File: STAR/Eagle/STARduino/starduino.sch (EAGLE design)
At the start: 80 parts, among them J3 J30J-15J30, J4 J30J-31J30, Q2 BSS8402DW, Q3 BSS8402DW, U1 SSCMNNN015PA2A3, U10 MC14504BDTG, U11 MAX31725MTA+, U12 TCA9535_RTW_24, U13 BMX055, U15 MC74VHC1GT125, U16 PCA9515A, U17 PCA9306DCT, U18 LT8616, U4 DS3231MZ+, U6 ATSAMD21G18, U8 ADXL375BCCZ

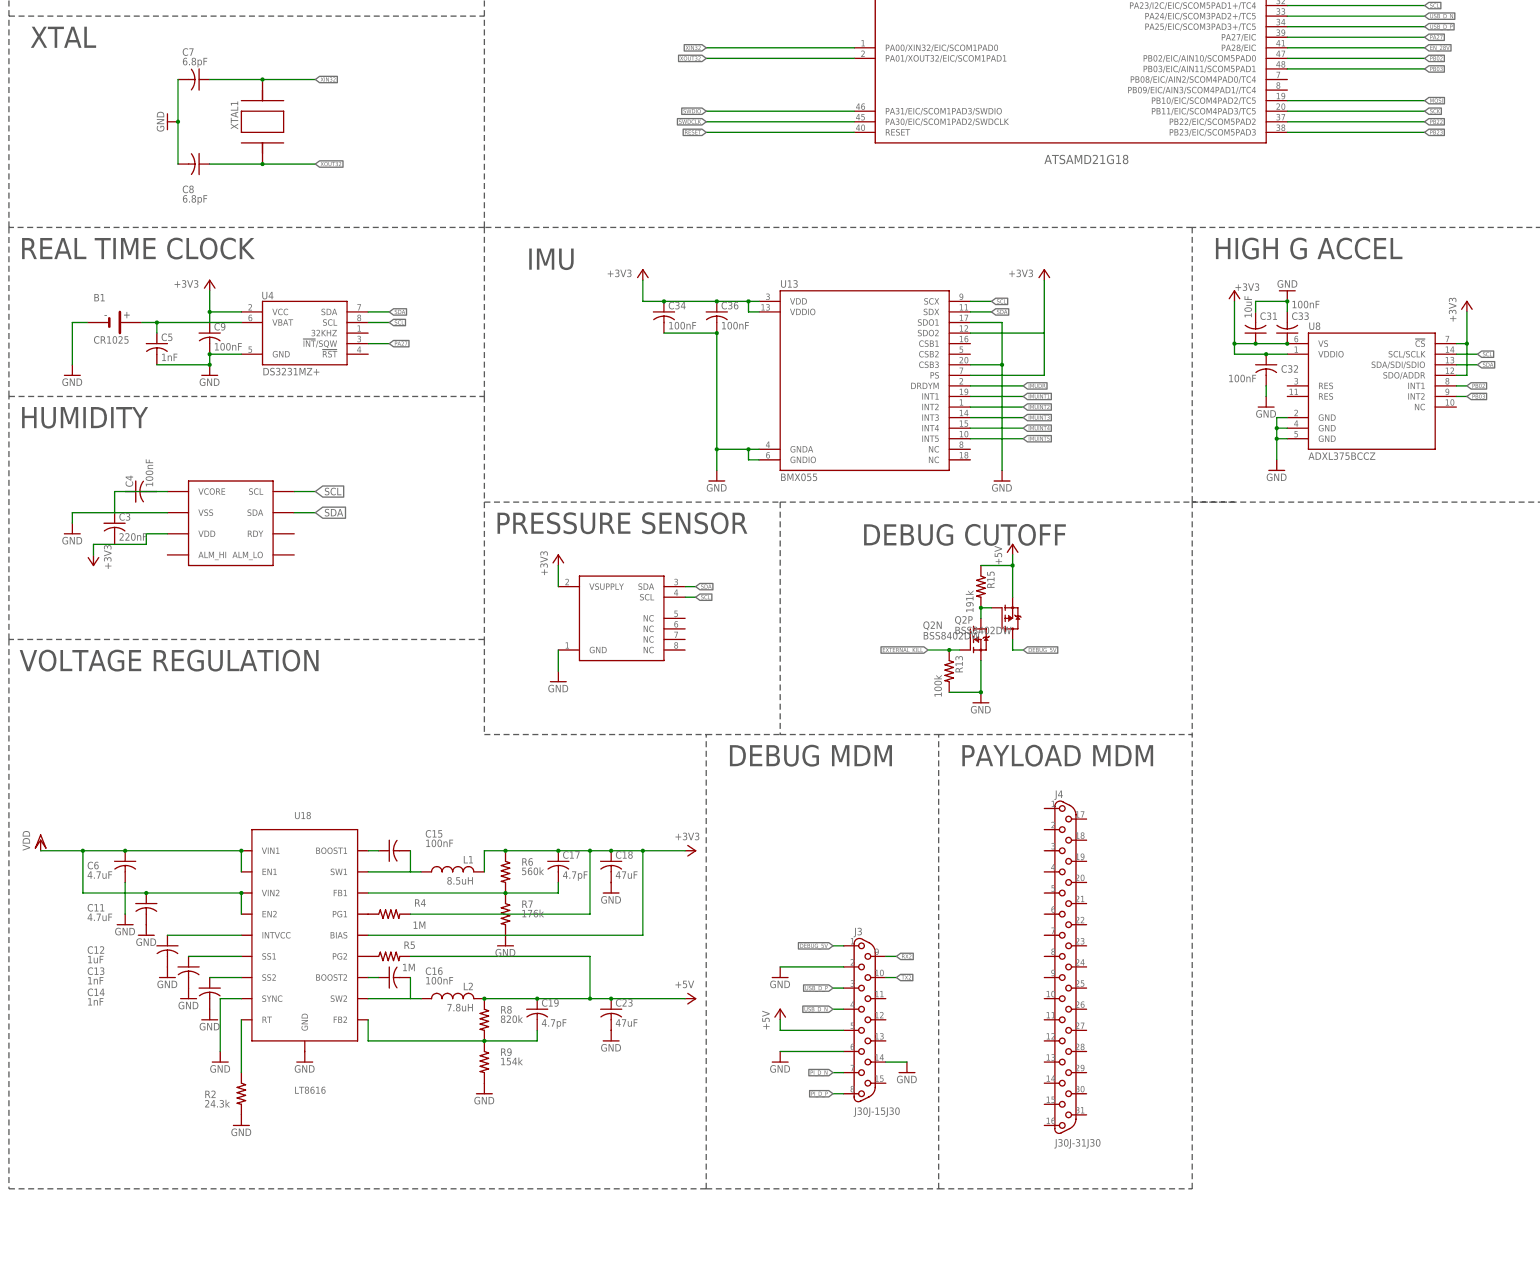
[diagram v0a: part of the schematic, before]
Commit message: datalogger differential pairs
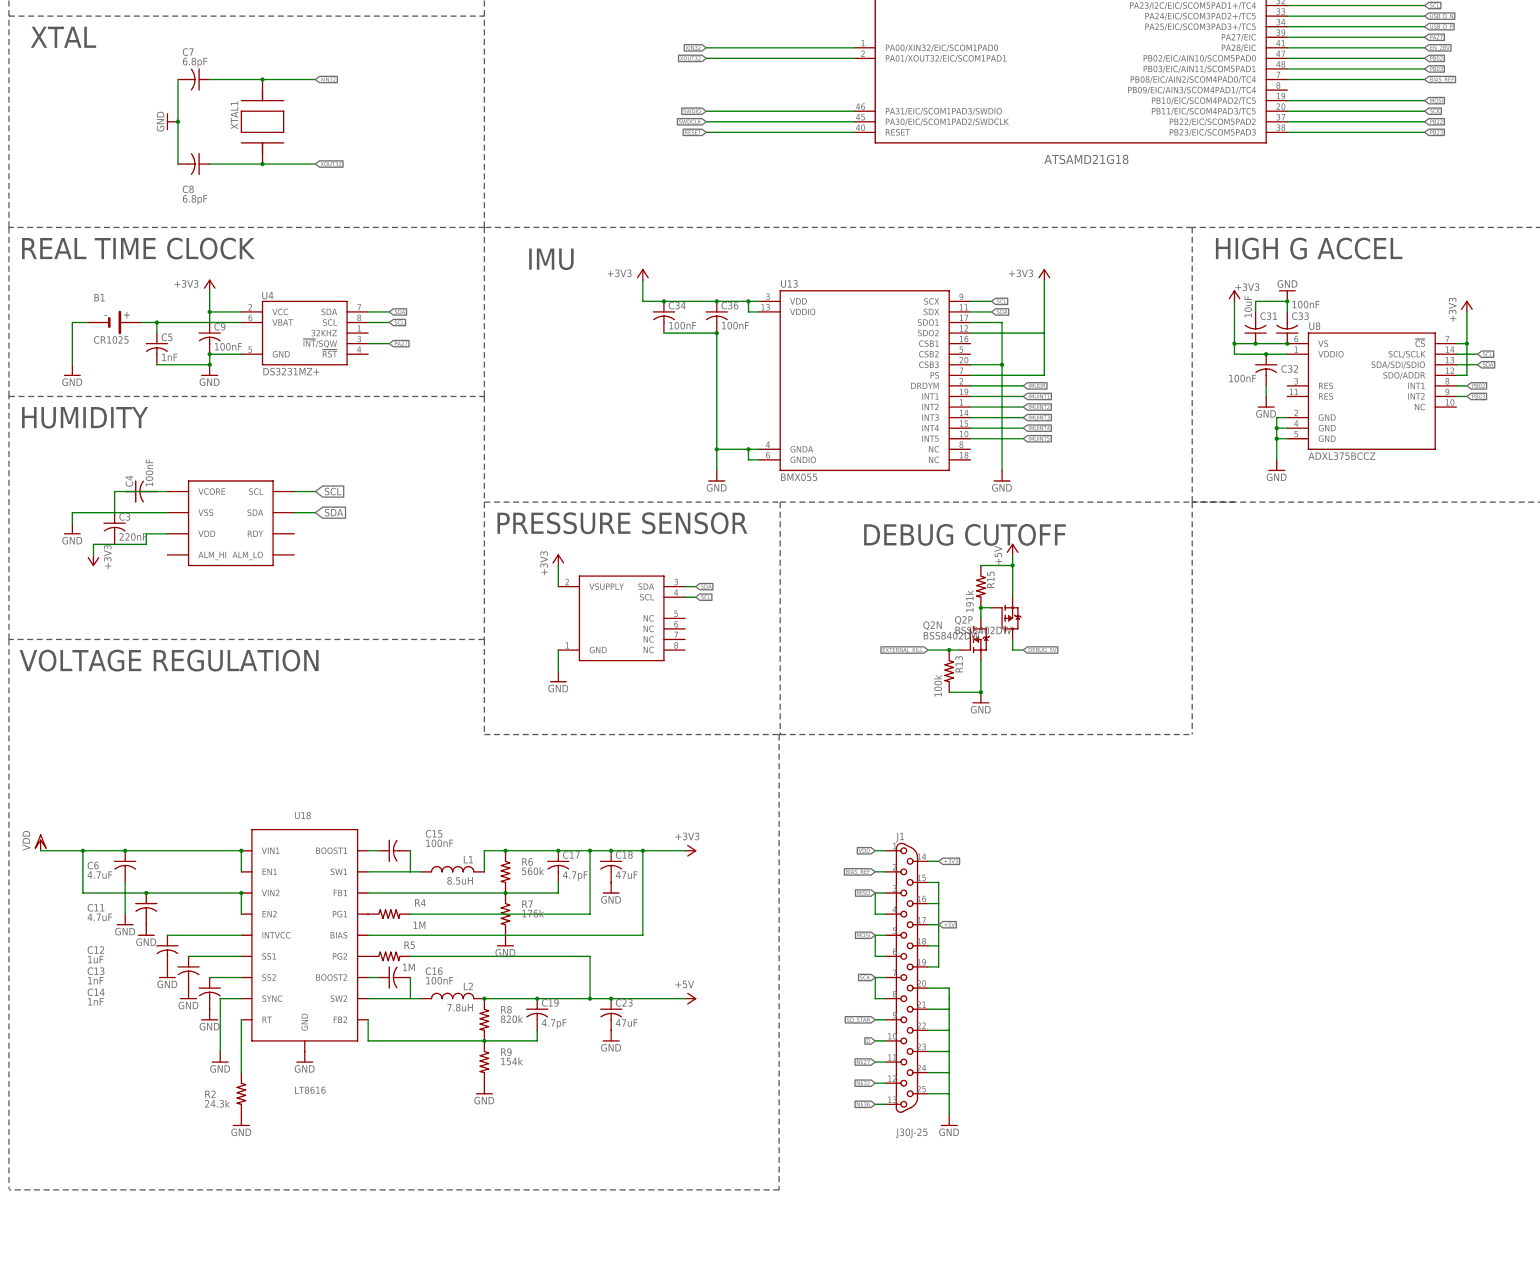
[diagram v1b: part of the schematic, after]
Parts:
- removed J3: J30J-15J30, CM_J30J:J30J-15J30
- removed J4: J30J-31J30, CM_J30J:J30J-31J30
- added J1: J30J-25, CM_J30J:J30J-25
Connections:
- removed net PI_D_N: J3.7
- removed net PI_D_P: J3.8
- new net BIAS_REF: J1.2, U6.PB08/EIC/AIN2/SCOM4PAD0/TC4
- new net D: J1.10
- new net N$27: J1.11
- new net N$32: J1.12
- new net N$36: J1.13
- new net SD_STAR: J1.9
- net +3V3: now also J1.14
- net +5V: now also J1.15, J1.16, J1.17, J1.18, J1.19; no longer J3.5
- net DEBUG_5V: no longer J3.1
- net GND: now also J1.20, J1.21, J1.22, J1.23, J1.24, J1.25; no longer J3.14, J3.2, J3.6
- net MISO: now also J1.3, J1.4
- net MOSI: now also J1.5, J1.6
- net RX2: no longer J3.9
- net SCK: now also J1.7, J1.8
- net TX2: no longer J3.10
- net USB_D_N: no longer J3.4
- net USB_D_P: no longer J3.3
- net VDD: now also J1.1
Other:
- note removed: "DEBUG MDM"
- note removed: "PAYLOAD MDM"

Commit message: got rid of old STARduino routing
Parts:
- removed Q3: BSS8402DW, transistor-fet:BSS8402DW
- removed R22: 100k, resistor:R-US_R0603
- removed R24: 191k, resistor:R-US_R0603
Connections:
- removed net EXTERNAL_3V3: Q3P.D
- removed net N$18: Q3N.D, Q3P.G, R24.2
- new net N$2: C4.2, U$3.VCORE
- net +3V3: no longer Q3P.S, R24.1
- net EXTERNAL_KILL: no longer Q3N.G, R22.1
- net GND: no longer C4.2, Q3N.S, R22.2, U$3.VCORE
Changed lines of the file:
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@@
 <part name="GND10" library="supply1" deviceset="GND" device=""/>
 <part name="+3V9" library="supply1" deviceset="+3V3" device=""/>
-<part name="+3V19" library="supply1" deviceset="+3V3" device=""/>
-<part name="GND22" library="supply1" deviceset="GND" device=""/>
-<part name="R22" library="resistor" deviceset="R-US_" device="R0603" value="100k"/>
-<part name="R24" library="resistor" deviceset="R-US_" device="R0603" value="191k"/>
 <part name="JP1" library="CM_passives" deviceset="JUMPER-2" device="PTH"/>
 <part name="U$2" library="images" deviceset="SSL" device=".3IN_SILK"/>
 <part name="U$1" library="images" deviceset="STAR" device=""/>
 <part name="R28" library="SparkFun-Passives" deviceset="RESISTOR-ARRAY" device="0603-ARV" value="4.7k"/>
-<part name="Q3" library="transistor-fet" deviceset="BSS8402DW" device=""/>
 <part name="Q2" library="transistor-fet" deviceset="BSS8402DW" device=""/>
 <part name="U16" library="CM_IC" deviceset="PCA9515A" device=""/>
@@
 <instance part="GND10" gate="1" x="533.4" y="375.92"/>
 <instance part="+3V9" gate="G$1" x="505.46" y="355.6"/>
-<instance part="+3V19" gate="G$1" x="436.88" y="314.96" rot="R90"/>
-<instance part="GND22" gate="1" x="459.74" y="297.18"/>
-<instance part="R22" gate="G$1" x="449.58" y="299.72" rot="R270"/>
-<instance part="R24" gate="G$1" x="469.9" y="307.34" rot="R270"/>
 <instance part="JP1" gate="A" x="43.18" y="365.76"/>
 <instance part="U$2" gate="G$1" x="546.1" y="48.26"/>
@@
 <instance part="R28" gate="C" x="391.16" y="304.8" rot="R90"/>
 <instance part="R28" gate="D" x="416.56" y="304.8" rot="R90"/>
-<instance part="Q3" gate="N" x="457.2" y="307.34"/>
-<instance part="Q3" gate="P" x="482.6" y="307.34"/>
 <instance part="Q2" gate="N" x="236.22" y="193.04"/>
 <instance part="Q2" gate="P" x="243.84" y="198.12"/>
@@
 <pinref part="R28" gate="A" pin="2"/>
 <pinref part="R28" gate="B" pin="2"/>
-</segment>
-<segment>
-<pinref part="+3V19" gate="G$1" pin="+3V3"/>
-<wire x1="439.42" y1="314.96" x2="469.9" y2="314.96" width="0.1524" layer="91"/>
-<wire x1="469.9" y1="314.96" x2="485.14" y2="314.96" width="0.1524" layer="91"/>
-<wire x1="485.14" y1="314.96" x2="485.14" y2="312.42" width="0.1524" layer="91"/>
-<pinref part="R24" gate="G$1" pin="1"/>
-<wire x1="469.9" y1="314.96" x2="469.9" y2="312.42" width="0.1524" layer="91"/>
-<junction x="469.9" y="314.96"/>
-<pinref part="Q3" gate="P" pin="S"/>
 </segment>
 <segment>
@@
 </segment>
 <segment>
-<pinref part="GND22" gate="1" pin="GND"/>
-<wire x1="459.74" y1="302.26" x2="459.74" y2="299.72" width="0.1524" layer="91"/>
-<pinref part="R22" gate="G$1" pin="2"/>
-<wire x1="449.58" y1="294.64" x2="454.66" y2="294.64" width="0.1524" layer="91"/>
-<wire x1="454.66" y1="294.64" x2="454.66" y2="302.26" width="0.1524" layer="91"/>
-<wire x1="454.66" y1="302.26" x2="459.74" y2="302.26" width="0.1524" layer="91"/>
-<pinref part="Q3" gate="N" pin="S"/>
-<junction x="459.74" y="302.26"/>
-</segment>
-<segment>
 <pinref part="C41" gate="G$1" pin="2"/>
 <pinref part="GND15" gate="1" pin="GND"/>
@@
 <wire x1="20.32" y1="223.52" x2="20.32" y2="220.98" width="0.1524" layer="91"/>
 <pinref part="GND13" gate="1" pin="GND"/>
-<pinref part="U$3" gate="G$1" pin="VCORE"/>
-<pinref part="C4" gate="G$1" pin="2"/>
-<wire x1="43.18" y1="228.6" x2="40.64" y2="228.6" width="0.1524" layer="91"/>
 <pinref part="C4" gate="G$1" pin="1"/>
-<wire x1="40.64" y1="228.6" x2="33.02" y2="228.6" width="0.1524" layer="91"/>
 <wire x1="33.02" y1="228.6" x2="30.48" y2="228.6" width="0.1524" layer="91"/>
 <wire x1="30.48" y1="228.6" x2="30.48" y2="223.52" width="0.1524" layer="91"/>
@@
 </segment>
 <segment>
-<pinref part="R22" gate="G$1" pin="1"/>
-<wire x1="454.66" y1="304.8" x2="449.58" y2="304.8" width="0.1524" layer="91"/>
-<wire x1="449.58" y1="304.8" x2="447.04" y2="304.8" width="0.1524" layer="91"/>
-<junction x="449.58" y="304.8"/>
-<label x="447.04" y="304.8" size="1.016" layer="95" rot="R180" xref="yes"/>
-<pinref part="Q3" gate="N" pin="G"/>
-</segment>
-<segment>
 <pinref part="U16" gate="G$1" pin="EN"/>
 <wire x1="500.38" y1="381" x2="497.84" y2="381" width="0.1524" layer="91"/>
@@
 <label x="508" y="340.36" size="1.016" layer="95" xref="yes"/>
 <pinref part="R28" gate="A" pin="1"/>
-</segment>
-</net>
-<net name="N$18" class="0">
-<segment>
-<wire x1="459.74" y1="312.42" x2="464.82" y2="312.42" width="0.1524" layer="91"/>
-<wire x1="464.82" y1="312.42" x2="464.82" y2="299.72" width="0.1524" layer="91"/>
-<pinref part="R24" gate="G$1" pin="2"/>
-<wire x1="464.82" y1="299.72" x2="469.9" y2="299.72" width="0.1524" layer="91"/>
-<wire x1="469.9" y1="299.72" x2="469.9" y2="302.26" width="0.1524" layer="91"/>
-<wire x1="469.9" y1="299.72" x2="480.06" y2="299.72" width="0.1524" layer="91"/>
-<wire x1="480.06" y1="299.72" x2="480.06" y2="309.88" width="0.1524" layer="91"/>
-<junction x="469.9" y="299.72"/>
-<pinref part="Q3" gate="P" pin="G"/>
-<pinref part="Q3" gate="N" pin="D"/>
-</segment>
-</net>
-<net name="EXTERNAL_3V3" class="0">
-<segment>
-<wire x1="485.14" y1="302.26" x2="485.14" y2="299.72" width="0.1524" layer="91"/>
-<wire x1="485.14" y1="299.72" x2="490.22" y2="299.72" width="0.1524" layer="91"/>
-<label x="490.22" y="299.72" size="1.016" layer="95" xref="yes"/>
-<pinref part="Q3" gate="P" pin="D"/>
 </segment>
 </net>
@@
 </segment>
 </net>
+<net name="N$2" class="0">
+<segment>
+<pinref part="C4" gate="G$1" pin="2"/>
+<pinref part="U$3" gate="G$1" pin="VCORE"/>
+<wire x1="43.18" y1="228.6" x2="40.64" y2="228.6" width="0.1524" layer="91"/>
+</segment>
+</net>

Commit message: half a routed STARduino
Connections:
- removed net N$13: C15.2
- removed net N$16: C16.2
- net GND: now also C3.1
- net N$14: now also C15.2
- net N$17: now also C16.2
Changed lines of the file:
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@@
 <wire x1="33.02" y1="228.6" x2="30.48" y2="228.6" width="0.1524" layer="91"/>
 <wire x1="30.48" y1="228.6" x2="30.48" y2="223.52" width="0.1524" layer="91"/>
+<pinref part="C3" gate="G$1" pin="1"/>
 </segment>
 <segment>
@@
 </segment>
 </net>
-<net name="N$13" class="0">
-<segment>
+<net name="N$14" class="0">
+<segment>
+<pinref part="U18" gate="G$1" pin="SW1"/>
+<wire x1="91.44" y1="137.16" x2="101.6" y2="137.16" width="0.1524" layer="91"/>
+<pinref part="L1" gate="G$1" pin="1"/>
 <pinref part="C15" gate="G$1" pin="2"/>
+<wire x1="101.6" y1="137.16" x2="104.14" y2="137.16" width="0.1524" layer="91"/>
 <wire x1="101.6" y1="142.24" x2="101.6" y2="137.16" width="0.1524" layer="91"/>
 </segment>
 </net>
-<net name="N$14" class="0">
-<segment>
-<pinref part="U18" gate="G$1" pin="SW1"/>
-<wire x1="91.44" y1="137.16" x2="104.14" y2="137.16" width="0.1524" layer="91"/>
-<pinref part="L1" gate="G$1" pin="1"/>
-</segment>
-</net>
-<net name="N$16" class="0">
-<segment>
+<net name="N$17" class="0">
+<segment>
+<pinref part="U18" gate="G$1" pin="SW2"/>
+<wire x1="91.44" y1="106.68" x2="101.6" y2="106.68" width="0.1524" layer="91"/>
+<pinref part="L2" gate="G$1" pin="1"/>
 <pinref part="C16" gate="G$1" pin="2"/>
+<wire x1="101.6" y1="106.68" x2="104.14" y2="106.68" width="0.1524" layer="91"/>
 <wire x1="101.6" y1="111.76" x2="101.6" y2="106.68" width="0.1524" layer="91"/>
 </segment>
 </net>
-<net name="N$17" class="0">
-<segment>
-<pinref part="U18" gate="G$1" pin="SW2"/>
-<wire x1="91.44" y1="106.68" x2="104.14" y2="106.68" width="0.1524" layer="91"/>
-<pinref part="L2" gate="G$1" pin="1"/>
-</segment>
-</net>
